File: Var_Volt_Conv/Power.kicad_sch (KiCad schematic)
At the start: 57 parts

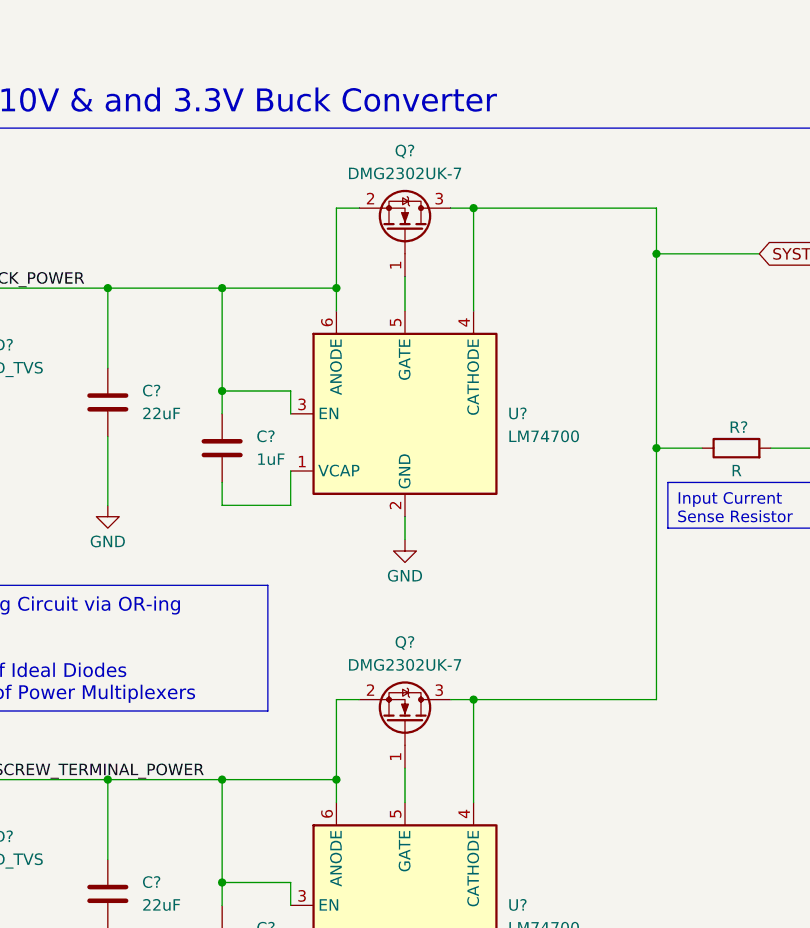
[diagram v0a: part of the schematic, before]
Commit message: Replaced Ideal OR transistors with IRFML8244TRPBF
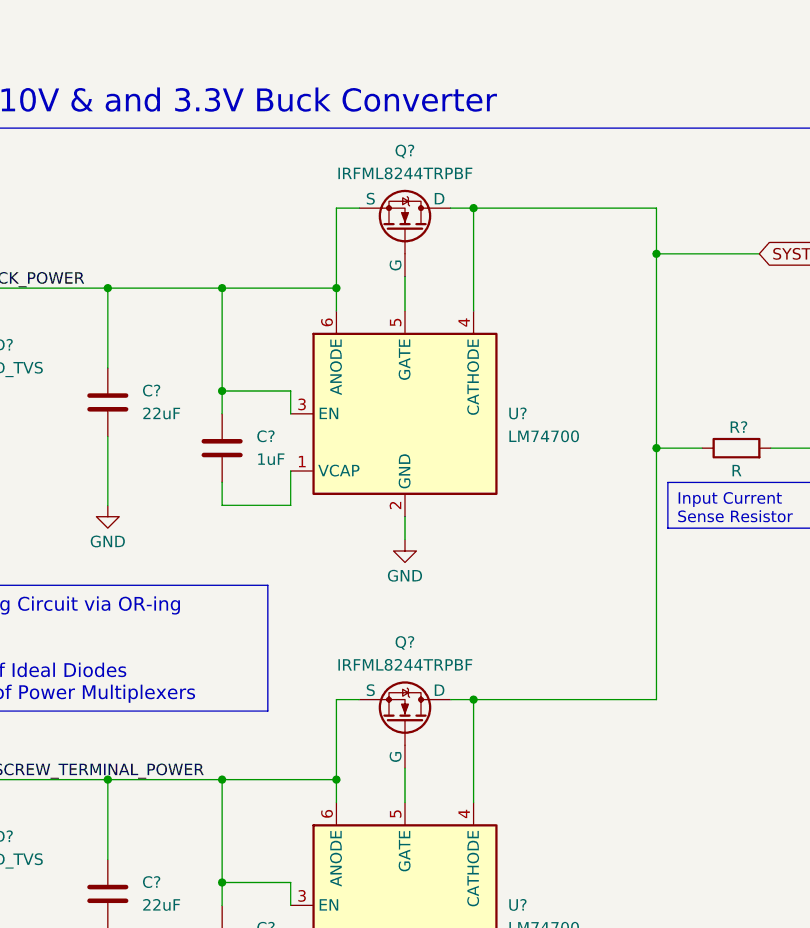
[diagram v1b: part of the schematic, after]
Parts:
- removed Q? (x2): DMG2302UK-7, Package_TO_SOT_SMD:SOT-23, symbol Transistor_FET:DMG2302U
- added Q? (x2): IRFML8244TRPBF, Package_TO_SOT_SMD:SOT-23, symbol Simulation_SPICE:NMOS
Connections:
- net JACK_POWER: now also Q?.2 (S)
- net SCREW_TERMINAL_POWER: now also Q?.2 (S)
- net SYSTEM_POWER_A: now also Q?.3 (D), Q?.3 (D)
- net at U?.5 (GATE): now also Q?.1 (G) (x2)
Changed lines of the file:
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@@
+	)
+	(symbol
+		(lib_id "Simulation_SPICE:NMOS")
+		(at 110.49 67.31 270)
+		(mirror x)
+		(unit 1)
+		(exclude_from_sim no)
+		(in_bom yes)
+		(on_board yes)
+		(dnp no)
+		(property "Reference" "Q?"
+			(at 110.49 58.42 90)
+			(effects
+				(font
+					(size 1.27 1.27)
+				)
+			)
+		)
+		(property "Value" "IRFML8244TRPBF"
+			(at 110.49 60.96 90)
+			(effects
+				(font
+					(size 1.27 1.27)
+				)
+			)
+		)
+		(property "Footprint" "Package_TO_SOT_SMD:SOT-23"
+			(at 113.03 62.23 0)
+			(effects
+				(font
+					(size 1.27 1.27)
+				)
+				(hide yes)
+			)
+		)
+		(property "Datasheet" "https://ngspice.sourceforge.io/docs/ngspice-html-manual/manual.xhtml#cha_MOSFETs"
+			(at 97.79 67.31 0)
+			(effects
+				(font
+					(size 1.27 1.27)
+				)
+				(hide yes)
+			)
+		)
+		(property "Description" "N-MOSFET transistor, drain/source/gate"
+			(at 110.49 67.31 0)
+			(effects
+				(font
+					(size 1.27 1.27)
+				)
+				(hide yes)
+			)
+		)
+		(property "Sim.Device" "NMOS"
+			(at 93.345 67.31 0)
+			(effects
+				(font
+					(size 1.27 1.27)
+				)
+				(hide yes)
+			)
+		)
+		(property "Sim.Type" "VDMOS"
+			(at 91.44 67.31 0)
+			(effects
+				(font
+					(size 1.27 1.27)
+				)
+				(hide yes)
+			)
+		)
+		(property "Sim.Pins" "1=D 2=G 3=S"
+			(at 95.25 67.31 0)
+			(effects
+				(font
+					(size 1.27 1.27)
+				)
+				(hide yes)
+			)
+		)
+		(pin "2"
+		)
+		(pin "1"
+		)
+		(pin "3"
+		)
+		(instances
+			(project ""
+				(path "/7c9580d6-c22f-4506-b9c3-9272e882c9fb/18589d04-92b7-4bb3-b941-112d31f9b6cf"
+					(reference "Q?")
+					(unit 1)
+				)
+			)
+		)
 	)
 	(symbol
@@
 	)
 	(symbol
-		(lib_id "Transistor_FET:DMG2302U")
-		(at 110.49 67.31 270)
-		(mirror x)
-		(unit 1)
-		(exclude_from_sim no)
-		(in_bom yes)
-		(on_board yes)
-		(dnp no)
-		(property "Reference" "Q?"
-			(at 110.49 58.42 90)
-			(effects
-				(font
-					(size 1.27 1.27)
-				)
-			)
-		)
-		(property "Value" "DMG2302UK-7"
-			(at 110.49 60.96 90)
-			(effects
-				(font
-					(size 1.27 1.27)
-				)
-			)
-		)
-		(property "Footprint" "Package_TO_SOT_SMD:SOT-23"
-			(at 108.585 62.23 0)
-			(effects
-				(font
-					(size 1.27 1.27)
-					(italic yes)
-				)
-				(justify left)
-				(hide yes)
-			)
-		)
-		(property "Datasheet" "http://www.diodes.com/assets/Datasheets/DMG2302U.pdf"
-			(at 106.68 62.23 0)
-			(effects
-				(font
-					(size 1.27 1.27)
-				)
-				(justify left)
-				(hide yes)
-			)
-		)
-		(property "Description" "4.2A Id, 20V Vds, N-Channel MOSFET, SOT-23"
-			(at 110.49 67.31 0)
-			(effects
-				(font
-					(size 1.27 1.27)
-				)
-				(hide yes)
-			)
-		)
-		(pin "2"
-		)
-		(pin "1"
-		)
-		(pin "3"
-		)
-		(instances
-			(project ""
-				(path "/7c9580d6-c22f-4506-b9c3-9272e882c9fb/18589d04-92b7-4bb3-b941-112d31f9b6cf"
-					(reference "Q?")
-					(unit 1)
-				)
-			)
-		)
-	)
-	(symbol
 		(lib_id "power:GND")
 		(at 331.47 110.49 0)
@@
 				(path "/7c9580d6-c22f-4506-b9c3-9272e882c9fb/18589d04-92b7-4bb3-b941-112d31f9b6cf"
 					(reference "#PWR036")
-					(unit 1)
-				)
-			)
-		)
-	)
-	(symbol
-		(lib_id "Transistor_FET:DMG2302U")
-		(at 110.49 121.92 270)
-		(mirror x)
-		(unit 1)
-		(exclude_from_sim no)
-		(in_bom yes)
-		(on_board yes)
-		(dnp no)
-		(property "Reference" "Q?"
-			(at 110.49 113.03 90)
-			(effects
-				(font
-					(size 1.27 1.27)
-				)
-			)
-		)
-		(property "Value" "DMG2302UK-7"
-			(at 110.49 115.57 90)
-			(effects
-				(font
-					(size 1.27 1.27)
-				)
-			)
-		)
-		(property "Footprint" "Package_TO_SOT_SMD:SOT-23"
-			(at 108.585 116.84 0)
-			(effects
-				(font
-					(size 1.27 1.27)
-					(italic yes)
-				)
-				(justify left)
-				(hide yes)
-			)
-		)
-		(property "Datasheet" "http://www.diodes.com/assets/Datasheets/DMG2302U.pdf"
-			(at 106.68 116.84 0)
-			(effects
-				(font
-					(size 1.27 1.27)
-				)
-				(justify left)
-				(hide yes)
-			)
-		)
-		(property "Description" "4.2A Id, 20V Vds, N-Channel MOSFET, SOT-23"
-			(at 110.49 121.92 0)
-			(effects
-				(font
-					(size 1.27 1.27)
-				)
-				(hide yes)
-			)
-		)
-		(pin "2"
-		)
-		(pin "1"
-		)
-		(pin "3"
-		)
-		(instances
-			(project "Var_Volt_Conv"
-				(path "/7c9580d6-c22f-4506-b9c3-9272e882c9fb/18589d04-92b7-4bb3-b941-112d31f9b6cf"
-					(reference "Q?")
 					(unit 1)
 				)
@@
 					(unit 1)
 				)
+			)
+		)
+	)
+	(symbol
+		(lib_id "Simulation_SPICE:NMOS")
+		(at 110.49 121.92 270)
+		(mirror x)
+		(unit 1)
+		(exclude_from_sim no)
+		(in_bom yes)
+		(on_board yes)
+		(dnp no)
+		(property "Reference" "Q?"
+			(at 110.49 113.03 90)
+			(effects
+				(font
+					(size 1.27 1.27)
+				)
+			)
+		)
+		(property "Value" "IRFML8244TRPBF"
+			(at 110.49 115.57 90)
+			(effects
+				(font
+					(size 1.27 1.27)
+				)
+			)
+		)
+		(property "Footprint" "Package_TO_SOT_SMD:SOT-23"
+			(at 113.03 116.84 0)
+			(effects
+				(font
+					(size 1.27 1.27)
+				)
+				(hide yes)
+			)
+		)
+		(property "Datasheet" "https://ngspice.sourceforge.io/docs/ngspice-html-manual/manual.xhtml#cha_MOSFETs"
+			(at 97.79 121.92 0)
+			(effects
+				(font
+					(size 1.27 1.27)
+				)
+				(hide yes)
+			)
+		)
+		(property "Description" "N-MOSFET transistor, drain/source/gate"
+			(at 110.49 121.92 0)
+			(effects
+				(font
+					(size 1.27 1.27)
+				)
+				(hide yes)
+			)
+		)
+		(property "Sim.Device" "NMOS"
+			(at 93.345 121.92 0)
+			(effects
+				(font
+					(size 1.27 1.27)
+				)
+				(hide yes)
+			)
+		)
+		(property "Sim.Type" "VDMOS"
+			(at 91.44 121.92 0)
+			(effects
+				(font
+					(size 1.27 1.27)
+				)
+				(hide yes)
+			)
+		)
+		(property "Sim.Pins" "1=D 2=G 3=S"
+			(at 95.25 121.92 0)
+			(effects
+				(font
+					(size 1.27 1.27)
+				)
+				(hide yes)
+			)
+		)
+		(pin "2"
+		)
+		(pin "1"
+		)
+		(pin "3"
+		)
+		(instances
+			(project "Var_Volt_Conv"
+				(path "/7c9580d6-c22f-4506-b9c3-9272e882c9fb/18589d04-92b7-4bb3-b941-112d31f9b6cf"
+					(reference "Q?")
+					(unit 1)
+				)

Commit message: Sourced TVS diodes for input system power
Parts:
- D?: footprint (none) -> Diode_SMD:D_SOD-882
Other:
- note added: "TVS Diodes: PESD18VF1BLYL"
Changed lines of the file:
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@@
 		)
 	)
+	(text "TVS Diodes: PESD18VF1BLYL"
+		(exclude_from_sim no)
+		(at 40.894 143.51 0)
+		(effects
+			(font
+				(size 1.27 1.27)
+			)
+		)
+	)
 	(text "[1] Power"
 		(exclude_from_sim no)
@@
 			)
 		)
-		(property "Footprint" ""
+		(property "Footprint" "Diode_SMD:D_SOD-882"
 			(at 62.23 81.28 0)
 			(effects

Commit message: Minor changes to auxilliary components of System Power sub-cictui
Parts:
- added C? (x2): 0.1uF, symbol Device:C
- C? (x2): value 1uF -> 0.1uF
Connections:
- net GND: now also C?.2, C?.2
- net SYSTEM_POWER_A: now also C?.1, C?.1

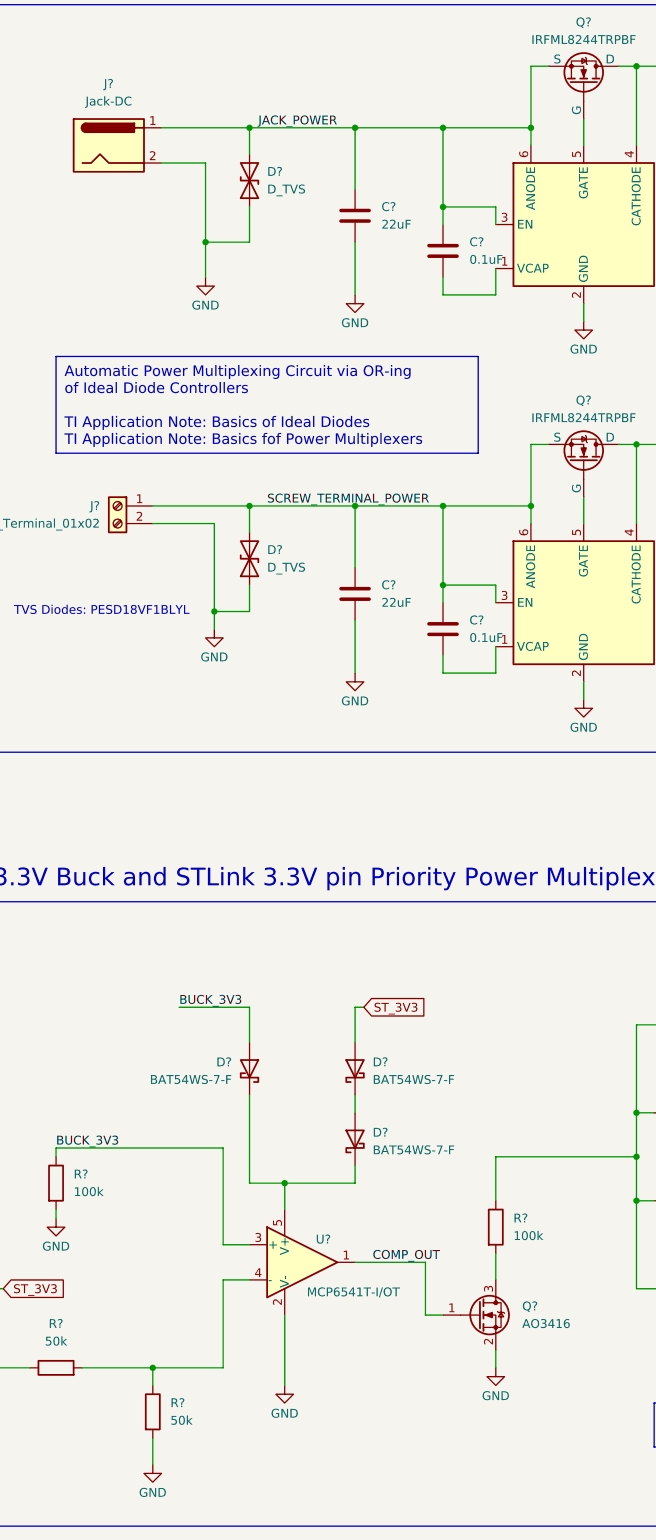
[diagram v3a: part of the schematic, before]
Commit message: Made notes on 3V3 priority power multiplexer circuit and minor corrections
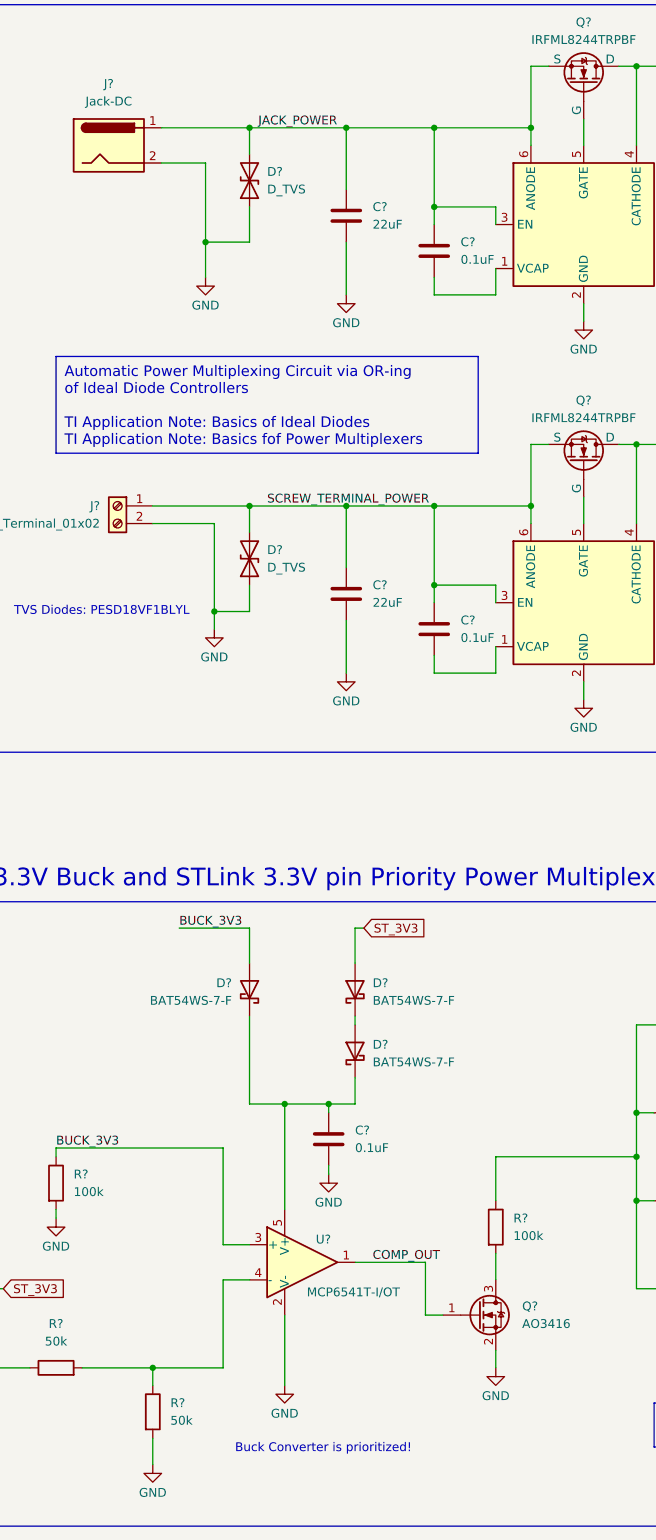
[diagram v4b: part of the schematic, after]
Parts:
- added C?: 0.1uF, symbol Device:C
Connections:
- net GND: now also C?.2
- net at D?.1 (K), D?.1 (K), U?.5 (V+): now also C?.1
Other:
- note added: "Buck Converter is prioritized!"
- moved on the sheet: C?, D?

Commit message: Done reviewing Buck-Boost converter circuit, made minor corrections
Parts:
- removed R?: 100k, symbol Device:R
- added C?: 10uF, symbol Device:C
- added C?: 240pF, symbol Device:C
- C?: value 22uF -> 10uF
- R?: value 10k -> 9.3k
- RV?: value R_Potentiometer -> 1M ADJ
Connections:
- net GND: now also C?.2, C?.2
- net SYSTEM_POWER_B: now also C?.1
- net at R?.1, U?.15 (COMP): now also C?.1
- no-connect marks 4 -> 5
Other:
- note added: "20uF effective capacitance is recommended Using parallel caps as 20uF ceramic is not readily available"
- note added: "9.3kohm resistance sets the switching frequency to 2MHz"
- note added: "Adjust Potentiometer to change output voltage from 1.32V to 20V"
- note added: "Mode Max input voltage is 3V3"
- note added: "Variable Power Output: 1.32V to 20V"
- note removed: "Cp = 7.07pF < 10pF Cp not necessary"
- note removed: "Variable Power Output: 1V to 20V"
- moved on the sheet: C?, D?, J?, L?, Q?, R?, RV?, U?

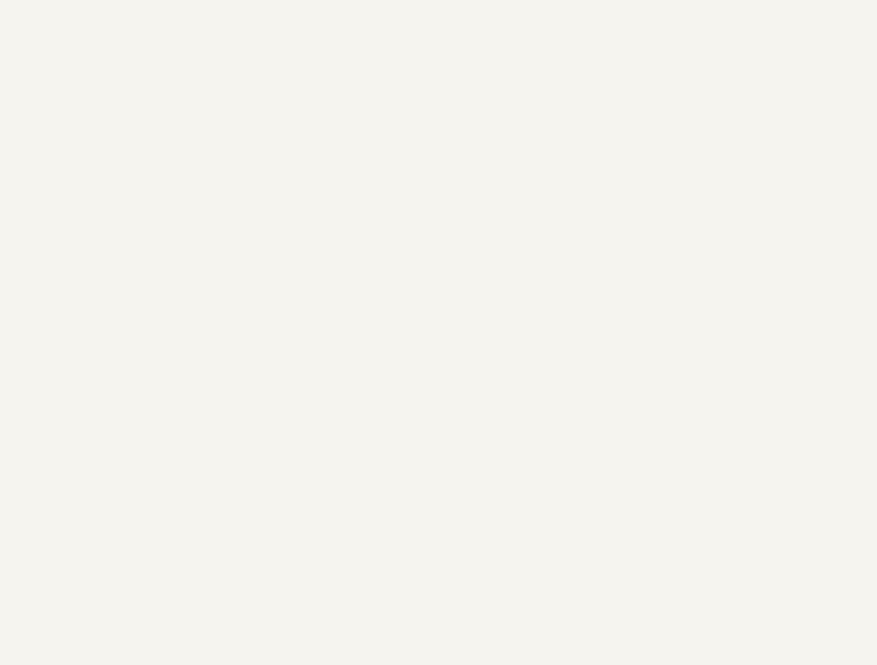
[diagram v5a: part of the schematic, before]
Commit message: LCD screen needs a nominal supply voltage of 3V, added a 3V LDOto the power circuitry, the LDO is powered by the buck converter
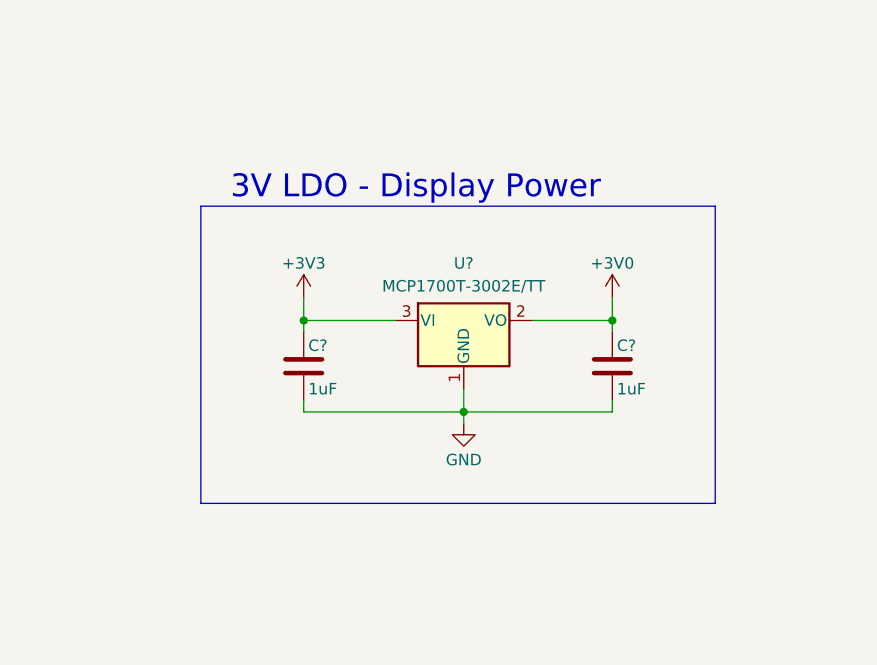
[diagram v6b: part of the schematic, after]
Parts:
- added C? (x2): 1uF, symbol Device:C
- added U?: MCP1700T-3002E/TT, Package_TO_SOT_SMD:SOT-23, symbol Regulator_Linear:MCP1700x-300xxTT
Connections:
- net +3V3: now also C?.1, U?.3 (VI)
- net GND: now also C?.2, C?.2, U?.1 (GND)
- new net +3V0: C?.1, U?.2 (VO)
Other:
- note added: "3V LDO - Display Power"

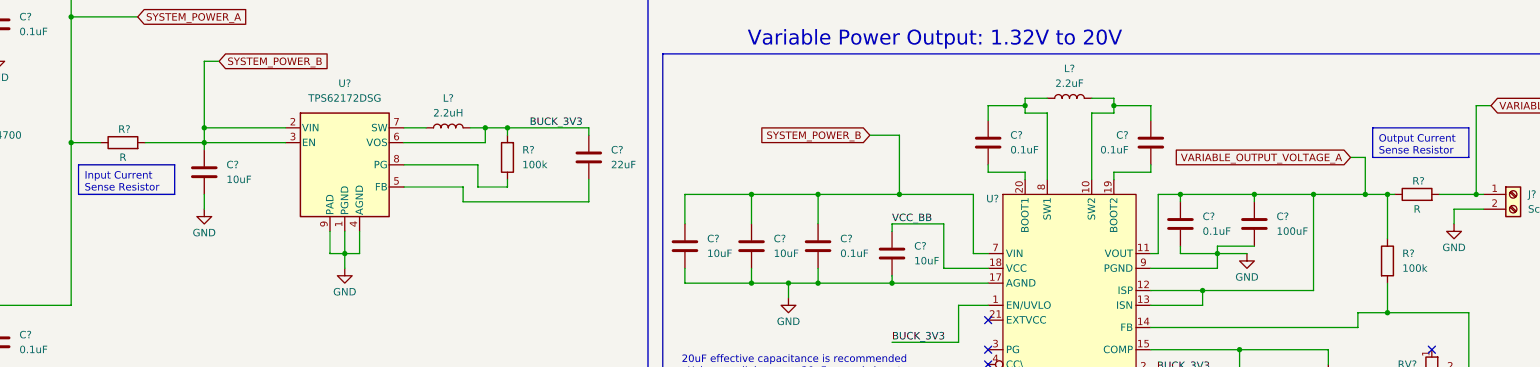
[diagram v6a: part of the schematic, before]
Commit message: Finalized current sensing circuit values
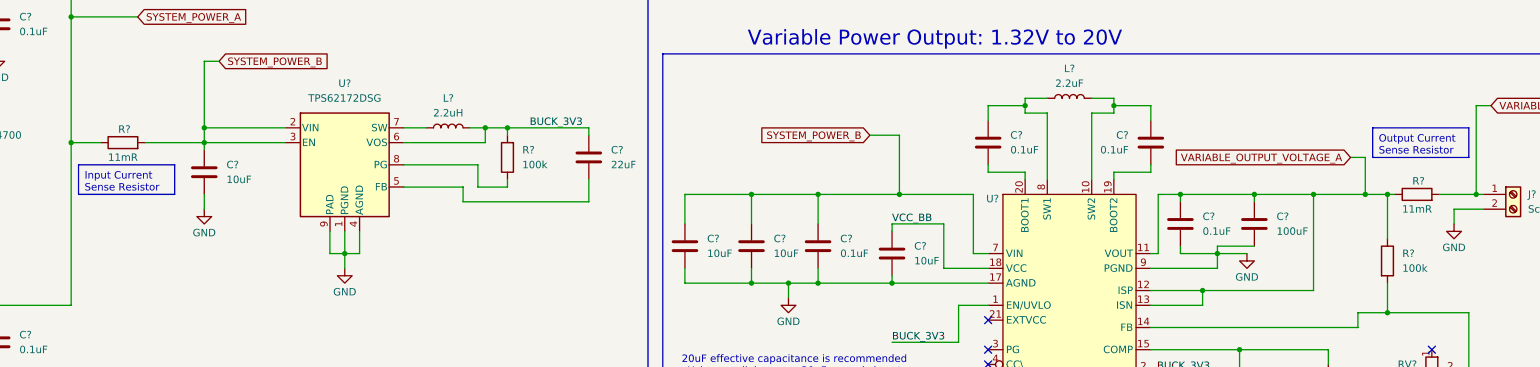
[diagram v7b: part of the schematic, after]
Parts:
- R? (x2): value R -> 11mR
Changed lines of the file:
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@@
 			)
 		)
-		(property "Value" "R"
+		(property "Value" "11mR"
 			(at 359.41 102.87 90)
 			(effects
@@
 			)
 		)
-		(property "Value" "R"
+		(property "Value" "11mR"
 			(at 137.16 93.98 90)
 			(effects
